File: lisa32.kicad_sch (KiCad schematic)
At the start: 16 parts, among them J1 DX07S016JA1R1500, J2 Conn_01x19, J3 Conn_01x19

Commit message: erc ok
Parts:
- added C23: 100nF/50V, symbol Device:C
- added D5: WS2812, LED_SMD:LED_WS2812_PLCC6_5.0x5.0mm_P1.6mm, symbol LED:WS2812
- added Q2: SS8050-G, Package_TO_SOT_SMD:SOT-23, symbol Transistor_BJT:BC817
- added R10, R11, R12, R23, R6, R7, R8, R9: 1k, symbol Device:R
- added R22: 150, symbol Device:R
- added R4, R5: 10k, symbol Device:R
- Q1: renamed from Q?; value BC817 -> SS8050-G
- gave numbers to parts that had none: 12
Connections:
- net +5V: now also D5.5 (VDD), R22.1
- net EN: now also Q1.3 (C), R12.2
- net GND: now also C23.2, D5.6 (VSS)
- net IO0: now also Q2.3 (C)
- net IO12: now also R8.2
- net IO13: now also R11.2
- net IO14: now also R10.2
- net IO15: now also R9.2
- net IO4: now also R23.1
- net RXD0: now also R6.2
- net TXD0: now also R7.2
- net USB to JTAG + UART/RXD: now also R7.1
- net USB to JTAG + UART/TCK: now also R11.1
- net USB to JTAG + UART/TDI: now also R8.1
- net USB to JTAG + UART/TDO: now also R9.1
- net USB to JTAG + UART/TMS: now also R10.1
- net USB to JTAG + UART/TXD: now also R6.1
- net USB to JTAG + UART/~TRST: now also R12.1
- net at Q1.1 (B): now also R4.2
- net ~RTS: now reaches Q1.2 (E)
- net ~RTS: now also R5.1
- new net: Q2.1 (B), R5.2
- new net: C23.1, D5.3 (VCC), R22.2
- new net: D5.2 (DIN), R23.2
- new net ~DTR: Q2.2 (E), R4.1
- no-connect marks 2 -> 7
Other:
- sheet ESP32 target ports: added CLK, CMD, EN, IO0, IO12, IO13, IO14, IO15, IO16, IO17, IO18, IO19, IO2, IO21, IO22, IO23, IO25, IO26, IO27, IO32, IO33, IO34, IO35, IO4, IO5, RXD0, SD0, SD1, SD2, SD3, SENSOR_VN, SENSOR_VP, TXD0; removed none
- moved on the sheet: C3, C4, Q1, SW1, SW2

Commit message: wip footprint assoc
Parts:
- C1, C2: footprint (none) -> Capacitor_SMD:C_1206_3216Metric
- C23, C3, C4: footprint (none) -> Capacitor_SMD:C_0603_1608Metric
- D1: footprint (none) -> Diode_SMD:D_SOD-323
- J2, J3: footprint (none) -> Connector_PinHeader_2.54mm:PinHeader_1x19_P2.54mm_Vertical

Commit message: placing test
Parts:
- R1, R10, R11, R12, R2, R22, R23, R3, R4, R5, R6, R7, R8, R9: footprint (none) -> Resistor_SMD:R_0603_1608Metric
- SW1, SW2: footprint (none) -> Button_Switch_SMD:SW_SPST_B3U-1000P

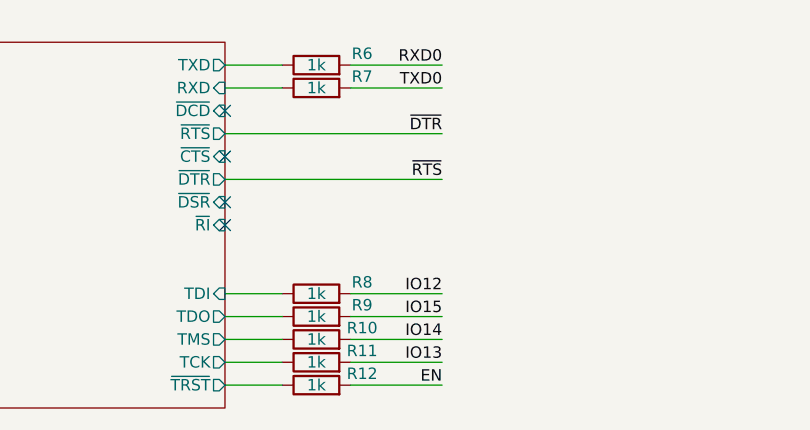
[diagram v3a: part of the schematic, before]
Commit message: fix autoprogram signals
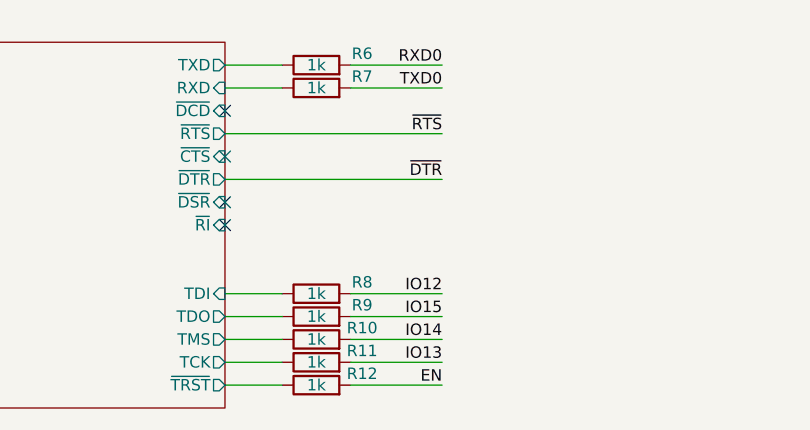
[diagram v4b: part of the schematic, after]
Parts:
- J1: footprint Connector_USB:USB_C_Receptacle_XKB_U262-16XN-4BVC11 -> Connector_USB:USB_C_Receptacle_HRO_TYPE-C-31-M-12
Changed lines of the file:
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@@
   (junction (at 257.81 90.17) (diameter 0.9144) (color 0 0 0 0))
   (junction (at 262.89 142.24) (diameter 0.9144) (color 0 0 0 0))
+  (no_connect (at 170.18 40.64))
+  (no_connect (at 52.07 67.31))
+  (no_connect (at 52.07 64.77))
   (no_connect (at 170.18 43.18))
-  (no_connect (at 52.07 64.77))
-  (no_connect (at 170.18 40.64))
-  (no_connect (at 170.18 30.48))
   (no_connect (at 170.18 35.56))
   (no_connect (at 57.15 179.07))
-  (no_connect (at 52.07 67.31))
+  (no_connect (at 170.18 30.48))
   (wire (pts (xy 25.4 179.07) (xy 29.21 179.07))
     (stroke (width 0) (type solid) (color 0 0 0 0))
@@
     (effects (font (size 1.27 1.27)) (justify right bottom))
   )
-  (label "~DTR" (at 194.31 33.02 180)
-    (effects (font (size 1.27 1.27)) (justify right bottom))
-  )
-  (label "~RTS" (at 194.31 38.1 180)
+  (label "~RTS" (at 194.31 33.02 180)
+    (effects (font (size 1.27 1.27)) (justify right bottom))
+  )
+  (label "~DTR" (at 194.31 38.1 180)
     (effects (font (size 1.27 1.27)) (justify right bottom))
   )
@@
     )
   )
-  (symbol (lib_id "Connector:USB_C_Receptacle_USB2.0") (at 36.83 52.07 0) (unit 1)
+  (symbol (lib_name "Connector:USB_C_Receptacle_USB2.0_1") (lib_id "Connector:USB_C_Receptacle_USB2.0") (at 36.83 52.07 0) (unit 1)
     (in_bom yes) (on_board yes)
     (property "Reference" "J1" (id 0) (at 36.83 30.48 0))
     (property "Value" "DX07S016JA1R1500" (id 1) (at 36.83 33.02 0))
-    (property "Footprint" "Connector_USB:USB_C_Receptacle_XKB_U262-16XN-4BVC11" (id 2) (at 40.64 52.07 0)
+    (property "Footprint" "Connector_USB:USB_C_Receptacle_HRO_TYPE-C-31-M-12" (id 2) (at 40.64 52.07 0)
       (effects (font (size 1.27 1.27)) hide)
     )
@@
       (reference "D5") (unit 1) (value "WS2812") (footprint "LED_SMD:LED_WS2812_PLCC6_5.0x5.0mm_P1.6mm")
     )
-    (path "/a1d24d3c-b21d-404f-9ef1-cf557c232066"
-      (reference "J1") (unit 1) (value "DX07S016JA1R1500") (footprint "Connector_USB:USB_C_Receptacle_XKB_U262-16XN-4BVC11")
+    (path "/0edcee65-01dc-41fa-99e5-440f88478b60"
+      (reference "J1") (unit 1) (value "DX07S016JA1R1500") (footprint "Connector_USB:USB_C_Receptacle_HRO_TYPE-C-31-M-12")
     )
     (path "/acd813c6-f658-4bd6-94ed-77eb77b80cd8"

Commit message: wip placing
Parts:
- added H1, H2, H3, H4: MountingHole, MountingHole:MountingHole_2.2mm_M2, symbol Mechanical:MountingHole
- J1: footprint Connector_USB:USB_C_Receptacle_HRO_TYPE-C-31-M-12 -> Connector_USB:USB_C_Receptacle_Palconn_UTC16-G
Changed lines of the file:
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@@
   (junction (at 257.81 90.17) (diameter 0.9144) (color 0 0 0 0))
   (junction (at 262.89 142.24) (diameter 0.9144) (color 0 0 0 0))
+  (no_connect (at 170.18 40.64))
+  (no_connect (at 57.15 179.07))
+  (no_connect (at 170.18 35.56))
+  (no_connect (at 52.07 67.31))
+  (no_connect (at 52.07 64.77))
   (no_connect (at 170.18 30.48))
-  (no_connect (at 52.07 64.77))
-  (no_connect (at 170.18 40.64))
   (no_connect (at 170.18 43.18))
-  (no_connect (at 170.18 35.56))
-  (no_connect (at 57.15 179.07))
-  (no_connect (at 52.07 67.31))
   (wire (pts (xy 25.4 179.07) (xy 29.21 179.07))
     (stroke (width 0) (type solid) (color 0 0 0 0))
@@
     )
     (property "Datasheet" "" (id 3) (at 257.81 123.19 0)
+      (effects (font (size 1.27 1.27)) hide)
+    )
+  )
+  (symbol (lib_id "Mechanical:MountingHole") (at 114.3 177.8 0) (unit 1)
+    (in_bom yes) (on_board yes)
+    (property "Reference" "H1" (id 0) (at 116.84 176.53 0)
+      (effects (font (size 1.27 1.27)) (justify left))
+    )
+    (property "Value" "MountingHole" (id 1) (at 118.11 179.07 0)
+      (effects (font (size 1.27 1.27)) (justify left) hide)
+    )
+    (property "Footprint" "MountingHole:MountingHole_2.2mm_M2" (id 2) (at 114.3 177.8 0)
+      (effects (font (size 1.27 1.27)) hide)
+    )
+    (property "Datasheet" "~" (id 3) (at 114.3 177.8 0)
+      (effects (font (size 1.27 1.27)) hide)
+    )
+  )
+  (symbol (lib_id "Mechanical:MountingHole") (at 114.3 182.88 0) (unit 1)
+    (in_bom yes) (on_board yes)
+    (property "Reference" "H2" (id 0) (at 116.84 181.61 0)
+      (effects (font (size 1.27 1.27)) (justify left))
+    )
+    (property "Value" "MountingHole" (id 1) (at 118.11 184.15 0)
+      (effects (font (size 1.27 1.27)) (justify left) hide)
+    )
+    (property "Footprint" "MountingHole:MountingHole_2.2mm_M2" (id 2) (at 114.3 182.88 0)
+      (effects (font (size 1.27 1.27)) hide)
+    )
+    (property "Datasheet" "~" (id 3) (at 114.3 182.88 0)
+      (effects (font (size 1.27 1.27)) hide)
+    )
+  )
+  (symbol (lib_id "Mechanical:MountingHole") (at 121.92 177.8 0) (unit 1)
+    (in_bom yes) (on_board yes)
+    (property "Reference" "H3" (id 0) (at 124.46 176.53 0)
+      (effects (font (size 1.27 1.27)) (justify left))
+    )
+    (property "Value" "MountingHole" (id 1) (at 125.73 179.07 0)
+      (effects (font (size 1.27 1.27)) (justify left) hide)
+    )
+    (property "Footprint" "MountingHole:MountingHole_2.2mm_M2" (id 2) (at 121.92 177.8 0)
+      (effects (font (size 1.27 1.27)) hide)
+    )
+    (property "Datasheet" "~" (id 3) (at 121.92 177.8 0)
+      (effects (font (size 1.27 1.27)) hide)
+    )
+  )
+  (symbol (lib_id "Mechanical:MountingHole") (at 121.92 182.88 0) (unit 1)
+    (in_bom yes) (on_board yes)
+    (property "Reference" "H4" (id 0) (at 124.46 181.61 0)
+      (effects (font (size 1.27 1.27)) (justify left))
+    )
+    (property "Value" "MountingHole" (id 1) (at 125.73 184.15 0)
+      (effects (font (size 1.27 1.27)) (justify left) hide)
+    )
+    (property "Footprint" "MountingHole:MountingHole_2.2mm_M2" (id 2) (at 121.92 182.88 0)
+      (effects (font (size 1.27 1.27)) hide)
+    )
+    (property "Datasheet" "~" (id 3) (at 121.92 182.88 0)
       (effects (font (size 1.27 1.27)) hide)
     )
@@
     (property "Reference" "J1" (id 0) (at 36.83 30.48 0))
     (property "Value" "DX07S016JA1R1500" (id 1) (at 36.83 33.02 0))
-    (property "Footprint" "Connector_USB:USB_C_Receptacle_HRO_TYPE-C-31-M-12" (id 2) (at 40.64 52.07 0)
+    (property "Footprint" "Connector_USB:USB_C_Receptacle_Palconn_UTC16-G" (id 2) (at 40.64 52.07 0)
       (effects (font (size 1.27 1.27)) hide)
     )
@@
       (reference "D5") (unit 1) (value "WS2812") (footprint "LED_SMD:LED_WS2812_PLCC6_5.0x5.0mm_P1.6mm")
     )
+    (path "/94cc81df-b72d-40f6-b8be-b8e5c84aef7d"
+      (reference "H1") (unit 1) (value "MountingHole") (footprint "MountingHole:MountingHole_2.2mm_M2")
+    )
+    (path "/a70925a8-a419-484b-8339-c874b2603c84"
+      (reference "H2") (unit 1) (value "MountingHole") (footprint "MountingHole:MountingHole_2.2mm_M2")
+    )
+    (path "/d0dcf18f-d281-421c-a9e3-e122293c22d3"
+      (reference "H3") (unit 1) (value "MountingHole") (footprint "MountingHole:MountingHole_2.2mm_M2")
+    )
+    (path "/dc5c19fe-ce76-4d76-8377-eb453d2fe369"
+      (reference "H4") (unit 1) (value "MountingHole") (footprint "MountingHole:MountingHole_2.2mm_M2")
+    )
     (path "/0edcee65-01dc-41fa-99e5-440f88478b60"
-      (reference "J1") (unit 1) (value "DX07S016JA1R1500") (footprint "Connector_USB:USB_C_Receptacle_HRO_TYPE-C-31-M-12")
+      (reference "J1") (unit 1) (value "DX07S016JA1R1500") (footprint "Connector_USB:USB_C_Receptacle_Palconn_UTC16-G")
     )
     (path "/acd813c6-f658-4bd6-94ed-77eb77b80cd8"

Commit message: routing completed
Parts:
- J1: value DX07S016JA1R1500 -> USB4105-GF-A
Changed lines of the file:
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@@
   (junction (at 262.89 142.24) (diameter 0.9144) (color 0 0 0 0))
   (no_connect (at 170.18 40.64))
-  (no_connect (at 57.15 179.07))
-  (no_connect (at 170.18 35.56))
+  (no_connect (at 170.18 43.18))
   (no_connect (at 52.07 67.31))
   (no_connect (at 52.07 64.77))
   (no_connect (at 170.18 30.48))
-  (no_connect (at 170.18 43.18))
+  (no_connect (at 57.15 179.07))
+  (no_connect (at 170.18 35.56))
   (wire (pts (xy 25.4 179.07) (xy 29.21 179.07))
     (stroke (width 0) (type solid) (color 0 0 0 0))
@@
     (in_bom yes) (on_board yes)
     (property "Reference" "J1" (id 0) (at 36.83 30.48 0))
-    (property "Value" "DX07S016JA1R1500" (id 1) (at 36.83 33.02 0))
+    (property "Value" "USB4105-GF-A" (id 1) (at 36.83 33.02 0))
     (property "Footprint" "Connector_USB:USB_C_Receptacle_Palconn_UTC16-G" (id 2) (at 40.64 52.07 0)
       (effects (font (size 1.27 1.27)) hide)
@@
     )
     (path "/0edcee65-01dc-41fa-99e5-440f88478b60"
-      (reference "J1") (unit 1) (value "DX07S016JA1R1500") (footprint "Connector_USB:USB_C_Receptacle_Palconn_UTC16-G")
+      (reference "J1") (unit 1) (value "USB4105-GF-A") (footprint "Connector_USB:USB_C_Receptacle_Palconn_UTC16-G")
     )
     (path "/acd813c6-f658-4bd6-94ed-77eb77b80cd8"
@@
       (reference "#PWR049") (unit 1) (value "GND") (footprint "")
     )
+    (path "/5f304c88-142b-41d9-b86f-2d4158492d4d/a04f630a-495d-4d28-9d66-738782f8f1f1"
+      (reference "#PWR0101") (unit 1) (value "GND") (footprint "")
+    )
     (path "/5f304c88-142b-41d9-b86f-2d4158492d4d/876fbf19-8b18-4393-a760-05c6d31f44d3"
       (reference "C5") (unit 1) (value "100nF/50V") (footprint "Capacitor_SMD:C_0603_1608Metric")
@@
       (reference "U4") (unit 1) (value "93C46") (footprint "Package_SO:SO-8_3.9x4.9mm_P1.27mm")
     )
-    (path "/5f304c88-142b-41d9-b86f-2d4158492d4d/f67005c3-8fd8-4174-8514-3e4781bd7e48"
-      (reference "Y1") (unit 1) (value "12MHz") (footprint "Crystal:Crystal_SMD_0603-2Pin_6.0x3.5mm")
+    (path "/5f304c88-142b-41d9-b86f-2d4158492d4d/32fbccdc-140b-45fb-8942-ec18d57e877b"
+      (reference "Y1") (unit 1) (value "12MHz") (footprint "Crystal:Crystal_SMD_3225-4Pin_3.2x2.5mm")
     )
     (path "/f1d8e85a-9ede-4ed8-b797-024e5aeb8973/05f0967b-6898-4a4c-8c60-9fff3569c37c"

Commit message: v0.1.0
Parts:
- C1, C2: PN (none) -> CL31A106KAHNNNE
- C23, C3, C4: PN (none) -> CL10B104KB8NNWC
- D1: PN (none) -> PMEG3020EJ
- D2: PN (none) -> PRTR5V0U2X,215
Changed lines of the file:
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@@
   (junction (at 257.81 90.17) (diameter 0.9144) (color 0 0 0 0))
   (junction (at 262.89 142.24) (diameter 0.9144) (color 0 0 0 0))
+  (no_connect (at 52.07 64.77))
+  (no_connect (at 52.07 67.31))
+  (no_connect (at 57.15 179.07))
+  (no_connect (at 170.18 30.48))
+  (no_connect (at 170.18 35.56))
   (no_connect (at 170.18 40.64))
   (no_connect (at 170.18 43.18))
-  (no_connect (at 52.07 67.31))
-  (no_connect (at 52.07 64.77))
-  (no_connect (at 170.18 30.48))
-  (no_connect (at 57.15 179.07))
-  (no_connect (at 170.18 35.56))
   (wire (pts (xy 25.4 179.07) (xy 29.21 179.07))
     (stroke (width 0) (type solid) (color 0 0 0 0))
@@
       (effects (font (size 1.27 1.27)) hide)
     )
+    (property "PN" "PMEG3020EJ" (id 4) (at 60.96 36.83 0)
+      (effects (font (size 1.27 1.27)) hide)
+    )
   )
   (symbol (lib_id "Device:C") (at 30.48 106.68 0) (unit 1)
@@
       (effects (font (size 1.27 1.27)) hide)
     )
+    (property "PN" "CL31A106KAHNNNE" (id 4) (at 30.48 106.68 0)
+      (effects (font (size 1.27 1.27)) hide)
+    )
   )
   (symbol (lib_id "Device:C") (at 63.5 106.68 0) (unit 1)
@@
       (effects (font (size 1.27 1.27)) hide)
     )
+    (property "PN" "CL31A106KAHNNNE" (id 4) (at 63.5 106.68 0)
+      (effects (font (size 1.27 1.27)) hide)
+    )
   )
   (symbol (lib_id "Device:C") (at 67.31 166.37 90) (unit 1)
@@
       (effects (font (size 1.27 1.27)) hide)
     )
+    (property "PN" "CL10B104KB8NNWC" (id 4) (at 67.31 166.37 0)
+      (effects (font (size 1.27 1.27)) hide)
+    )
   )
   (symbol (lib_id "Device:C") (at 227.33 147.32 90) (unit 1)
@@
       (effects (font (size 1.27 1.27)) hide)
     )
+    (property "PN" "CL10B104KB8NNWC" (id 4) (at 227.33 147.32 0)
+      (effects (font (size 1.27 1.27)) hide)
+    )
   )
   (symbol (lib_id "Device:C") (at 256.54 147.32 90) (unit 1)
@@
     )
     (property "Datasheet" "~" (id 3) (at 256.54 147.32 0)
+      (effects (font (size 1.27 1.27)) hide)
+    )
+    (property "PN" "CL10B104KB8NNWC" (id 4) (at 256.54 147.32 0)
       (effects (font (size 1.27 1.27)) hide)
     )
@@
       (effects (font (size 1.27 1.27)) hide)
     )
+    (property "PN" "PRTR5V0U2X,215" (id 4) (at 83.82 76.2 0)
+      (effects (font (size 1.27 1.27)) hide)
+    )
